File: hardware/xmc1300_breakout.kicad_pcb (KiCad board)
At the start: 2 copper layers, 50 x 45 mm, 26 parts, among them P1 CON-SENSOR2, P2 BOOT, P3 CONN_01X12, P4 CONN_01X12, P5 CONN_01X12, P6 CONN_01X12, P7 CONN_02X04, U1 XMC1XXX24, U2 DRILL, U3 DRILL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

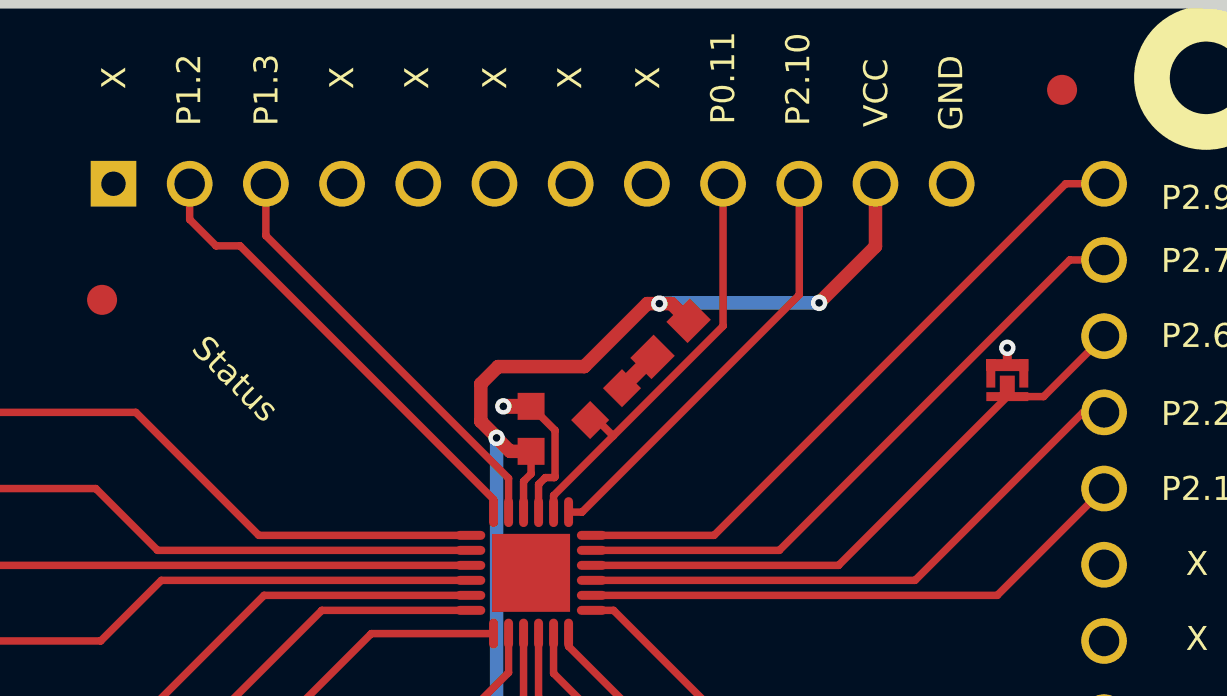
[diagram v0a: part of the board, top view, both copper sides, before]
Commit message: Fix BootPad & add status marking for status LED
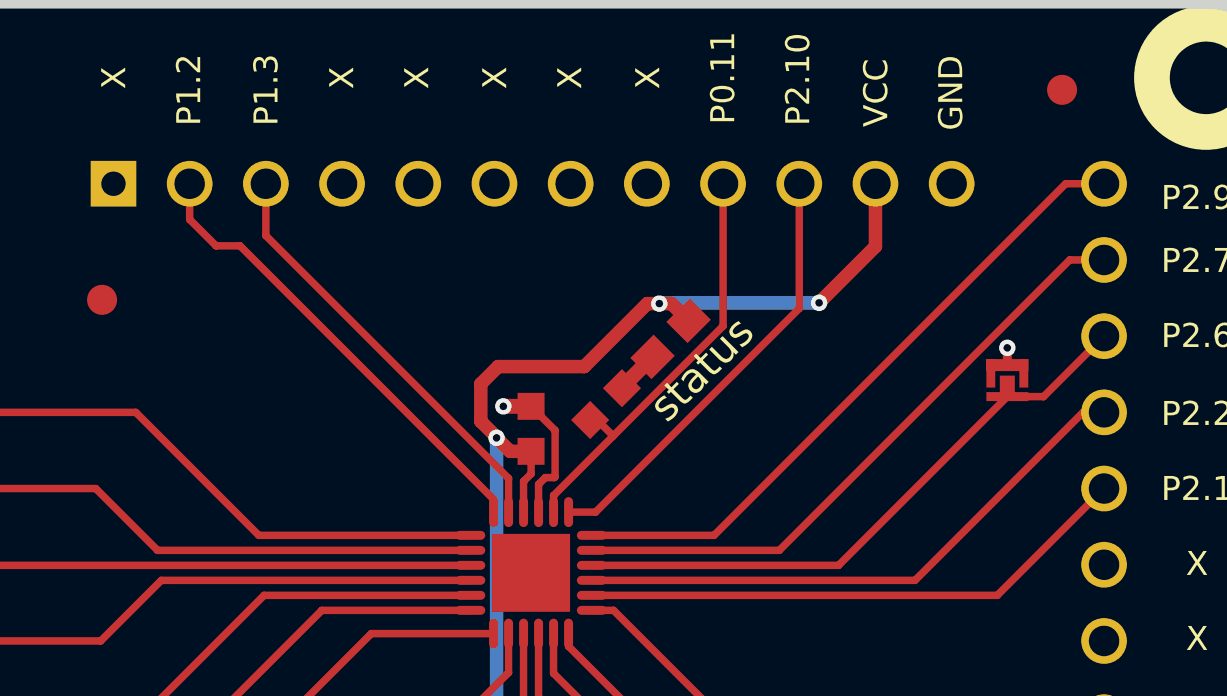
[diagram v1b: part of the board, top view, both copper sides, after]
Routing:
- net GND: track 23.7 -> 25.4 mm
- net Pin34: track 20.2 -> 21.8 mm
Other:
- board text added: "status"
- board text removed: "Status"
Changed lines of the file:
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@@
   (general
     (links 67)
-    (no_connects 7)
+    (no_connects 4)
     (area 120.109499 82.909499 170.490501 128.290501)
     (thickness 1.6002)
     (drawings 72)
-    (tracks 187)
+    (tracks 200)
     (zones 0)
     (modules 26)
@@
   (layers
     (0 Vorderseite signal)
-    (31 Rückseite signal)
+    (31 Rückseite signal hide)
     (32 B.Adhes user)
     (33 F.Adhes user)
@@
   )
   (setup
-    (last_trace_width 0.25)
+    (last_trace_width 0.2)
     (user_trace_width 0.25)
     (user_trace_width 0.29972)
@@
     )
   )
+  (gr_text status (at 150.99 95.31 45) (layer F.SilkS)
+    (effects (font (size 1 1) (thickness 0.15)))
+  )
   (gr_text ___ (at 139.925 111.8) (layer F.SilkS)
     (effects (font (size 2.032 1.524) (thickness 0.3048)))
@@
   (gr_line (start 122.8 83.1) (end 167.8 83.1) (angle 90) (layer Edge.Cuts) (width 0.381))
   (gr_arc (start 167.8 125.6) (end 170.3 125.6) (angle 90) (layer Edge.Cuts) (width 0.381))
-  (gr_text Status (at 134.2 94.4 315) (layer F.SilkS)
-    (effects (font (size 0.8 0.8) (thickness 0.15)) (justify left))
-  )
   (gr_line (start 167.8 128.1) (end 122.8 128.1) (angle 90) (layer Edge.Cuts) (width 0.381))
   (gr_arc (start 122.8 125.6) (end 122.8 128.1) (angle 90) (layer Edge.Cuts) (width 0.381))
@@
     (effects (font (size 0.8001 0.8001) (thickness 0.14986)))
   )
+  (segment (start 161.18 95.18) (end 161.175 95.175) (width 0.2) (layer Vorderseite) (net 1))
+  (segment (start 161.71 95.18) (end 161.18 95.18) (width 0.2) (layer Vorderseite) (net 1))
+  (segment (start 161.725 95.195) (end 161.71 95.18) (width 0.2) (layer Vorderseite) (net 1))
+  (segment (start 161.725 95.45) (end 161.725 95.195) (width 0.2) (layer Vorderseite) (net 1))
+  (segment (start 160.625 95.45) (end 160.625 95.215) (width 0.2) (layer Vorderseite) (net 1))
+  (segment (start 160.625 95.215) (end 160.65 95.19) (width 0.2) (layer Vorderseite) (net 1))
+  (segment (start 160.65 95.19) (end 161.19 95.19) (width 0.2) (layer Vorderseite) (net 1))
+  (segment (start 161.19 95.19) (end 161.175 95.175) (width 0.2) (layer Vorderseite) (net 1))
   (segment (start 161.175 95.175) (end 161.175 94.6) (width 0.29972) (layer Vorderseite) (net 1))
   (via (at 161.175 94.6) (size 0.55) (drill 0.25) (layers Vorderseite Rückseite) (net 1))
@@
   (segment (start 136.225 100.85) (end 132.125 96.75) (width 0.25) (layer Vorderseite) (net 23))
   (segment (start 126.3 91.67) (end 126.3 91.7) (width 0.25) (layer Vorderseite) (net 25))
-  (segment (start 146.55 100.075) (end 147 100.075) (width 0.25) (layer Vorderseite) (net 27))
-  (segment (start 154.24 92.835) (end 154.24 89.13) (width 0.25) (layer Vorderseite) (net 27))
-  (segment (start 147 100.075) (end 154.24 92.835) (width 0.25) (layer Vorderseite) (net 27))
+  (segment (start 146.55 100.075) (end 147.45 100.075) (width 0.25) (layer Vorderseite) (net 27))
+  (segment (start 154.24 93.285) (end 154.24 89.13) (width 0.25) (layer Vorderseite) (net 27))
+  (segment (start 147.45 100.075) (end 154.24 93.285) (width 0.25) (layer Vorderseite) (net 27))
   (segment (start 147.26967 97.00533) (end 147.50533 97.00533) (width 0.25) (layer Vorderseite) (net 28))
   (segment (start 147.50533 97.00533) (end 148.0375 97.5375) (width 0.25) (layer Vorderseite) (net 28))
@@
   (segment (start 158.1 102.35) (end 163.7 96.75) (width 0.25) (layer Vorderseite) (net 40))
   (segment (start 163.7 96.75) (end 164.4 96.75) (width 0.25) (layer Vorderseite) (net 40))
-  (segment (start 161.175 96.225) (end 162.385 96.225) (width 0.25) (layer Vorderseite) (net 41))
+  (segment (start 162.37 96.22) (end 162.37 96.225) (width 0.2) (layer Vorderseite) (net 41))
+  (segment (start 161.25 96.22) (end 162.37 96.22) (width 0.2) (layer Vorderseite) (net 41))
+  (segment (start 161.175 96.145) (end 161.25 96.22) (width 0.2) (layer Vorderseite) (net 41))
+  (segment (start 161.175 95.825) (end 161.175 96.145) (width 0.2) (layer Vorderseite) (net 41))
+  (segment (start 162.37 96.225) (end 162.385 96.225) (width 0.25) (layer Vorderseite) (net 41))
+  (segment (start 161.175 96.225) (end 162.37 96.225) (width 0.25) (layer Vorderseite) (net 41))
   (segment (start 162.385 96.225) (end 164.4 94.21) (width 0.25) (layer Vorderseite) (net 41))
   (segment (start 147.325 101.85) (end 155.55 101.85) (width 0.25) (layer Vorderseite) (net 41))

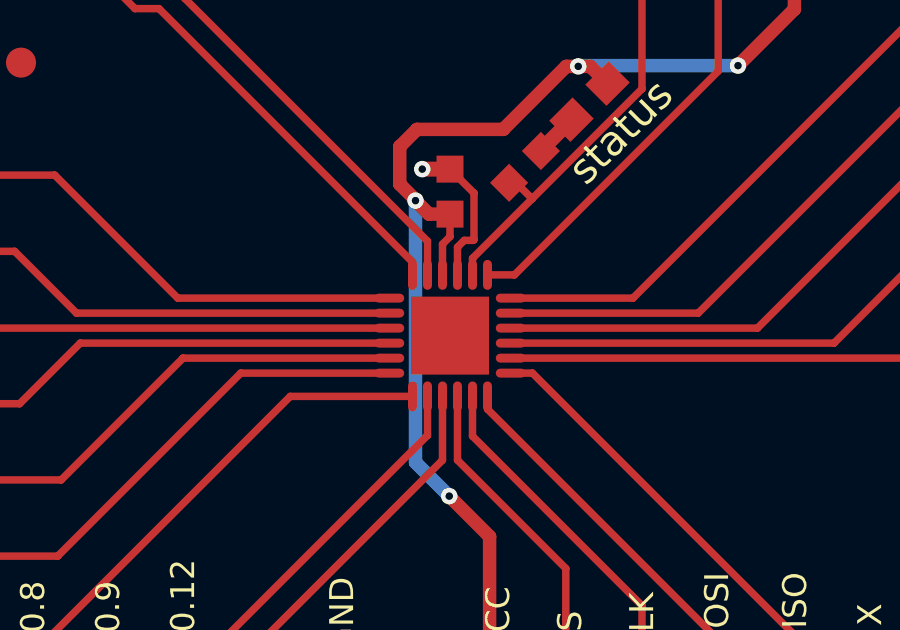
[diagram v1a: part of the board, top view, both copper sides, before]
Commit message: Fix GND path under MCU
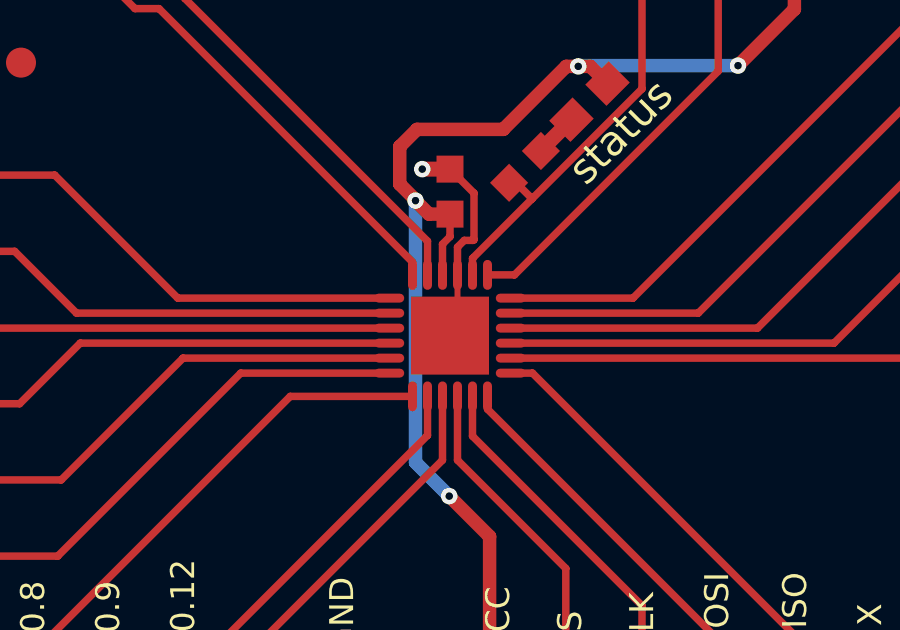
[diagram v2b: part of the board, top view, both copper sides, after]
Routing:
- net GND: track 25.4 -> 34.0 mm
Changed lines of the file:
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@@
   (general
     (links 67)
-    (no_connects 4)
-    (area 120.109499 82.909499 170.490501 128.290501)
+    (no_connects 0)
+    (area 119.445139 82.245139 282.895869 162.490743)
     (thickness 1.6002)
     (drawings 72)
-    (tracks 200)
+    (tracks 207)
     (zones 0)
     (modules 26)
@@
     (effects (font (size 0.8001 0.8001) (thickness 0.14986)))
   )
+  (segment (start 145.55 100.075) (end 145.55 101.05) (width 0.2) (layer Vorderseite) (net 1))
+  (segment (start 145.55 101.05) (end 145.95 101.45) (width 0.2) (layer Vorderseite) (net 1))
+  (segment (start 145.95 101.45) (end 144.65 102.75) (width 0.2) (layer Vorderseite) (net 1))
+  (segment (start 144.65 102.75) (end 144.65 101.45) (width 0.2) (layer Vorderseite) (net 1))
+  (segment (start 144.65 101.45) (end 145.95 101.45) (width 0.2) (layer Vorderseite) (net 1))
+  (segment (start 145.95 101.45) (end 145.95 102.75) (width 0.2) (layer Vorderseite) (net 1))
+  (segment (start 145.95 102.75) (end 144.65 102.75) (width 0.2) (layer Vorderseite) (net 1))
   (segment (start 161.18 95.18) (end 161.175 95.175) (width 0.2) (layer Vorderseite) (net 1))
   (segment (start 161.71 95.18) (end 161.18 95.18) (width 0.2) (layer Vorderseite) (net 1))
